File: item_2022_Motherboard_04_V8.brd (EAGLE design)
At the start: 160 x 100 mm, 50 parts, among them IC1 MCP602SN, IC2 LD117AS33TR, IC4 MCP6S26, U1 ESP32-DEVKITC-32D, U2 ADS1256_BOARD, U3 SSD1306_128X64, X1 MSTBA4, X2 MSTBA4

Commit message: aggiunta su sch condizionamento coppie
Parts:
- removed JP1: (no value), pinhead:1X08
- removed JP2: (no value), pinhead:2X04
- added C12, C13, C15, C20, C29: 100nF, rcl_LargePads:C0805
- added C14: 10uF / 16V, rcl_LargePads:PANASONIC_C
- added C16, C17, C18, C19: 3.3uF/50V, rcl_LargePads:C0805
- added C21, C23, C25, C27: 2.2uF, rcl_LargePads:C0805
- added C22, C24, C26, C28: 1uF, rcl_LargePads:C0805
- added C30: 100nF, rcl:C0805
- added D2, D3, D4, D5: BZW06-10B, diode_LargePads:F126Z12
- added GND, GND36: TPTP18SQ, testpad:TP18SQ
- added IC3: MCP1525TO, MCP1525_MCP1541:TO92
- added IC5, IC6, IC9: MCP6004SO, MCP6002_MCP6004:SO14
- added IC7: MCP3204SL, MCP3204_MCP3208:SO14
- added IC8: LM336LP, linear:TO92
- added R10, R11: 6.8k, rcl_LargePads:R0805
- added R12, R14, R22, R37, R39, R41, R43: 3.3k, rcl_LargePads:R0805
- added R13, R19, R21, R23: 5.6k, rcl_LargePads:R0805
- added R20: 3.3k, rcl_LargePads:M0805
- added R24, R26, R28, R30: 2.7k, rcl_LargePads:R0805
- added R25, R27, R29, R31: 82, rcl_LargePads:R0805
- added R32, R33, R34, R35: 1.8k, rcl_LargePads:R0805
- added R36, R38, R40, R42: 1.5k, rcl_LargePads:R0805
- added R44: 2.7k, rcl:R0805
- added R45, R46, R47, R48: 47, rcl:R0805
- added R49: 10k, rcl:R0805
- added TP13, TP7, TP8: TPTP16R, testpad:TP16R
- added TP14, TP15, TP16, TP17, TP18, TP19, TP20, TP21: TPTP14R, testpad:TP14R
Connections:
- removed net 3V3: U1.1
- removed net ADC_HALF_VREF: IC4.8, JP1.1, R16.1, R18.1, R2.1, R4.1, TP9.TP
- new net +2.5V: IC9.13, IC9.14, R32.1
- new net +3.3V_B: R49.2, U1.1
- new net ADC_HALF_VREF_A: IC4.8, IC9.8, IC9.9, R2.1, R4.1, TP13.TP, TP9.TP
- new net ADC_HALF_VREF_B: IC9.1, IC9.2, R16.1, R18.1
- new net ADC_VREF: IC7.13, IC9.6, IC9.7
- new net A_SPEED1: C25.2, IC6.8, IC6.9, IC7.3, TP20.TP
- new net A_SPEED2: C27.2, IC6.13, IC6.14, IC7.4, TP21.TP
- new net A_TORQUE1: C21.2, IC6.1, IC6.2, IC7.1, TP18.TP
- new net A_TORQUE2: C23.2, IC6.6, IC6.7, IC7.2, TP19.TP
- new net EN/!RESET!: C30.2, R49.1, U1.2
- new net N$1: C15.1, IC9.10, IC9.3, R10.1, R11.2
- new net N$15: R12.1, R13.2
- new net N$16: R14.1, R19.2
- new net N$17: R20.1, R21.2
- new net N$18: R22.1, R23.2
- new net N$19: R24.2, R25.1
- new net N$20: C16.1, IC5.3, R13.1, R24.1, R32.2, TP14.TP
- new net N$22: R26.2, R27.1
- new net N$23: R28.2, R29.1
- new net N$24: R30.2, R31.1
- new net N$25: C17.1, IC5.5, R19.1, R26.1, R33.2, TP15.TP
- new net N$26: C18.1, IC5.10, R21.1, R28.1, R34.2, TP16.TP
- new net N$27: C19.1, IC5.12, R23.1, R30.1, R35.2, TP17.TP
- new net N$28: IC5.1, IC5.2, R36.1
- new net N$29: IC5.6, IC5.7, R38.1
- new net N$30: IC5.8, IC5.9, R40.1
- new net N$31: IC5.13, IC5.14, R42.1
- new net N$32: C21.1, R36.2, R37.1
- new net N$33: C22.1, IC6.3, R37.2
- new net N$34: C23.1, R38.2, R39.1
- new net N$35: C24.1, IC6.5, R39.2
- new net N$36: C25.1, R40.2, R41.1
- new net N$37: C26.1, IC6.10, R41.2
- new net N$38: C27.1, R42.2, R43.1
- new net N$39: C28.1, IC6.12, R43.2
- new net N$40: R48.1, U1.27
- new net N$41: IC7.11, R45.1
- new net N$42: IC7.9, R46.1
- new net N$43: IC7.8, R47.1
- new net VREF: C14.+, IC3.2, IC8.2, IC9.12, IC9.5, R10.2, R44.1, TP8.TP
- net !CS_MCP3204!: now also R47.2; no longer JP1.5
- net +3V3: now also C29.1, IC7.14; no longer JP1.2
- net +5V: now also C12.1, C13.1, C20.1, IC3.3, IC5.4, IC6.4, IC9.4, R44.2, TP7.TP; no longer JP1.3
- net GND: now also C12.2, C13.2, C14.-, C15.2, C16.2, C17.2, C18.2, C19.2, C20.2, C22.2, C24.2, C26.2, C28.2, C29.2, D2.C, D3.C, D4.C, D5.C, GND.TP, GND36.TP, IC3.1, IC5.11, IC6.11, IC7.12, IC7.7, IC8.3, IC9.11, R11.1, R25.2, R27.2, R29.2, R31.2; no longer JP1.4
- net SPEED1+: now also D3.A, R20.2; no longer JP2.6
- net SPEED1-: no longer JP2.5
- net SPEED2+: now also D4.A, R22.2; no longer JP2.8
- net SPEED2-: no longer JP2.7
- net TORQUE1+: now also D5.A, R12.2; no longer JP2.2
- net TORQUE1-: no longer JP2.1
- net TORQUE2+: now also D2.A, R14.2; no longer JP2.4
- net TORQUE2-: no longer JP2.3
- net VSPI_MISO: now also IC7.10, R48.2; no longer JP1.7, U1.27
- net VSPI_MOSI: now also R46.2; no longer JP1.8
- net VSPI_SCK: now also R45.2; no longer JP1.6
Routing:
- net ADC_HALF_VREF: track 144.2 -> 0.00 mm, vias 5 -> 0
- net ADC_HALF_VREF_A: track 0.00 -> 144.2 mm, vias 0 -> 5

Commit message: aggiunta su brd cond coppie da sbrogliare
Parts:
- moved R47 266.2 mm to (157.6, 75.8), turned to 90 degrees
- moved R46 259.5 mm to (153.7, 75.8), turned to 90 degrees
- moved R45 252.7 mm to (149.8, 75.8), turned to 90 degrees
- moved TP7 237.9 mm to (121.9, 86.9)
- moved C30 235.8 mm to (21.3, 85.6), turned to 90 degrees
- moved R49 234.5 mm to (21.5, 89.7), turned to 90 degrees
- moved R42 227.9 mm to (151.1, 50.8), turned to 90 degrees
- moved R43 227.3 mm to (151.1, 55.2), turned to 90 degrees
- moved C29 225.9 mm to (142.3, 68.8), turned to 90 degrees
- moved TP13 223.0 mm to (124.4, 62.8)
- moved R48 221.3 mm to (46.5, 77.4), turned to 90 degrees
- moved GND 217.1 mm to (154.7, 84.4)
- moved C14 215.8 mm to (123.2, 82.5), turned to 180 degrees
- moved R44 213.1 mm to (118.7, 67.3), turned to 90 degrees
- moved TP8 210.5 mm to (119.1, 59.6)
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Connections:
- removed net SPEED1-: PL1.11
- removed net SPEED2-: PL1.13
- removed net TORQUE1-: PL1.7
- removed net TORQUE2-: PL1.9
- net +2.5V: now also R33.1, R34.1, R35.1
- net GND: now also C30.1, PL1.11, PL1.13, PL1.7, PL1.9
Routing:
- net SPEED2-: track 142.9 -> 0.00 mm, vias 1 -> 0
- net TORQUE1-: track 128.9 -> 0.00 mm, vias 2 -> 0
- net SPEED1-: track 122.9 -> 0.00 mm
- net TORQUE2-: track 118.3 -> 0.00 mm, vias 3 -> 0
- net SPEED2+: track 115.6 -> 0.00 mm, vias 2 -> 0
- net SPEED1+: track 109.6 -> 0.00 mm, vias 1 -> 0
- net TORQUE2+: track 107.0 -> 0.00 mm, vias 1 -> 0
- net TORQUE1+: track 96.3 -> 0.00 mm, vias 2 -> 0
- net VSPI_MISO: track 203.6 -> 124.8 mm
- net GND: track 792.1 -> 716.3 mm
- net VSPI_MOSI: track 241.5 -> 188.5 mm
- net ADC_HALF_VREF_A: track 144.2 -> 104.9 mm
- net +5V: track 195.0 -> 179.3 mm
- net +3V3: track 249.1 -> 241.9 mm
- removed copper zone on layer 1, net GND
- removed copper zone on layer 16, net GND
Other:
- board text removed: "CONDIZIONAMENTO COPPIE - VELOCITA'"

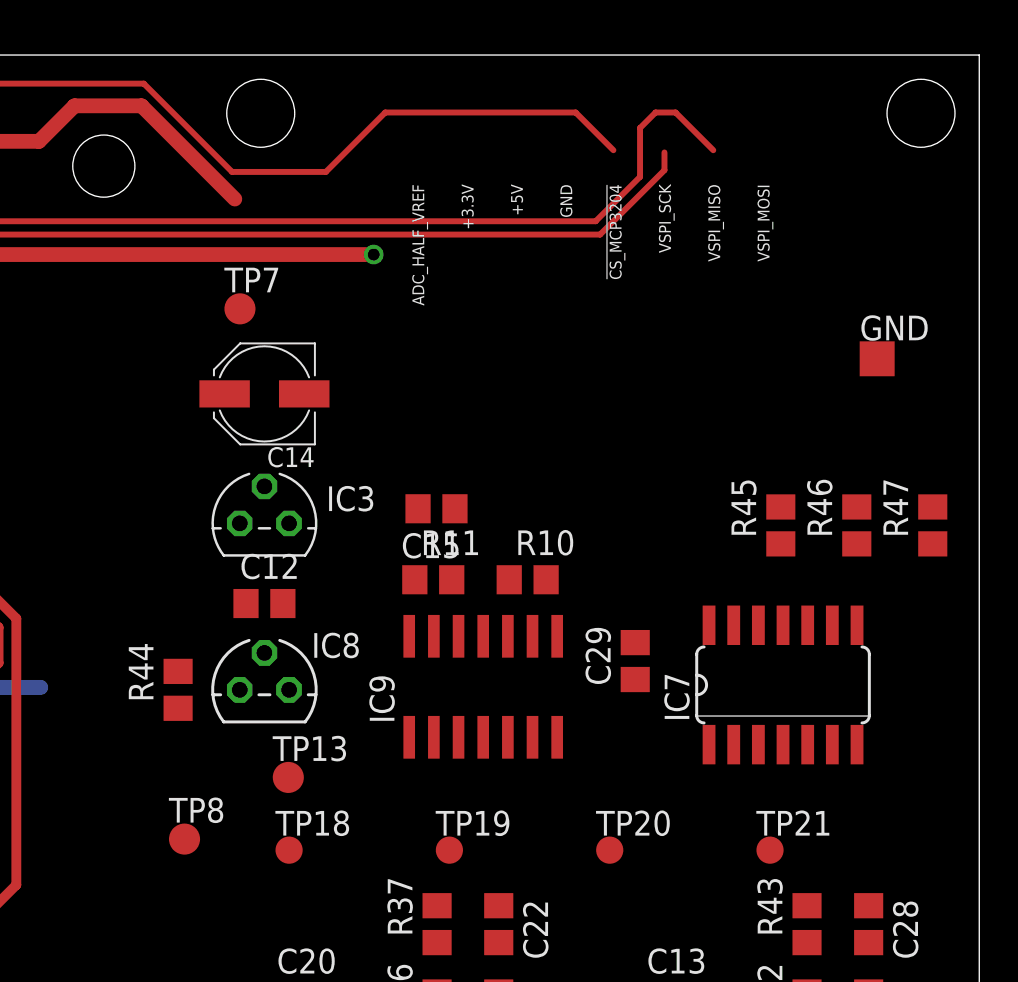
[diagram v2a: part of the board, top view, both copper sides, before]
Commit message: place pcb components on grid
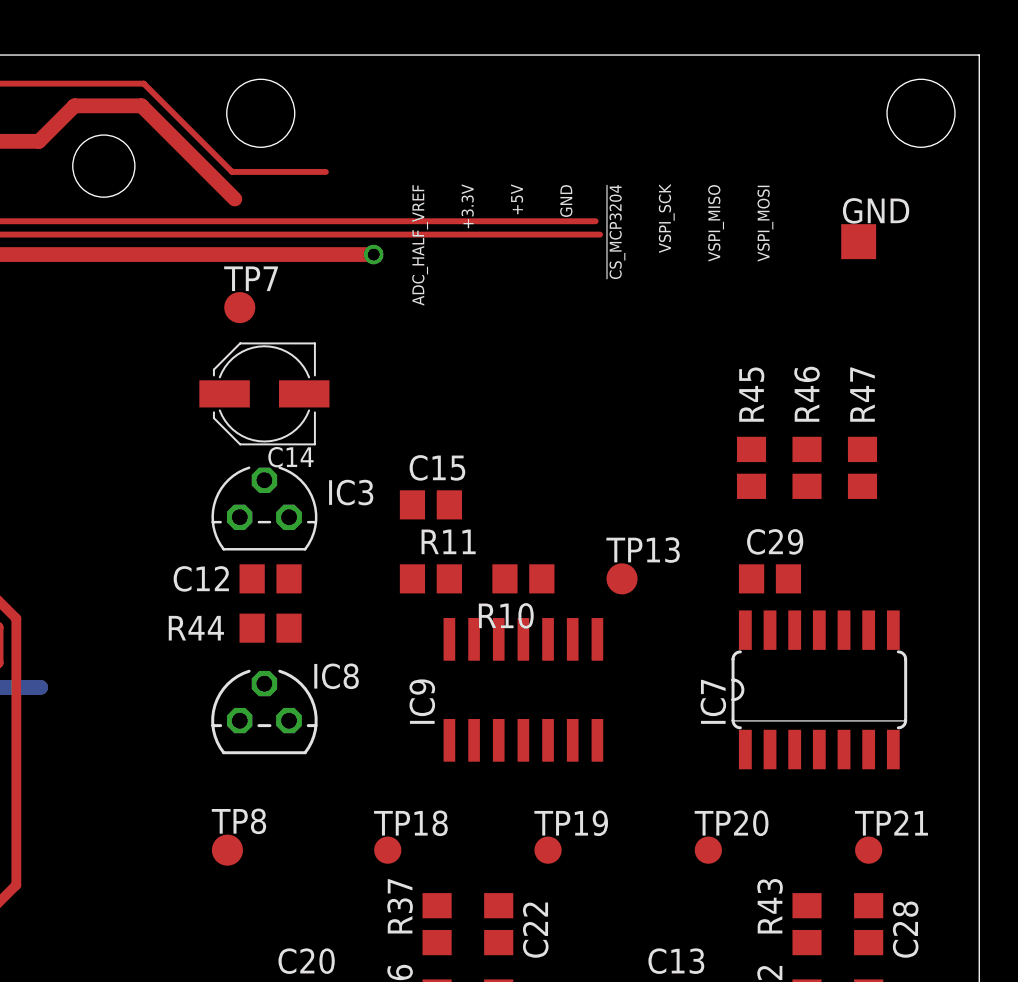
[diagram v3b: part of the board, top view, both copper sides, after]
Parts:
- moved TP13 20.0 mm to (141.6, 73.0)
- moved C29 8.13 mm to (149.2, 73.0), turned to 0 degrees
- moved GND 6.11 mm to (153.8, 90.4)
- moved R44 5.72 mm to (123.5, 70.5), turned to 180 degrees
- moved TP20 5.08 mm to (146.1, 59.1)
- moved TP21 5.08 mm to (154.3, 59.1)
- moved TP18 5.08 mm to (129.5, 59.1)
- moved TP19 5.08 mm to (137.8, 59.1)
- moved R47 4.68 mm to (154.0, 78.7)
- moved R46 3.92 mm to (151.1, 78.7)
- moved R45 3.32 mm to (148.3, 78.7)
- moved TP8 2.28 mm to (121.3, 59.1)
- moved IC9 2.08 mm to (136.5, 67.3)
- moved IC7 1.89 mm to (151.8, 67.3)
- moved IC8 1.59 mm to (123.2, 65.7)
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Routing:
- net !CS_MCP3204!: track 167.4 -> 150.5 mm
- net VSPI_MISO: track 124.8 -> 114.2 mm
- net VSPI_SCK: track 223.6 -> 218.0 mm

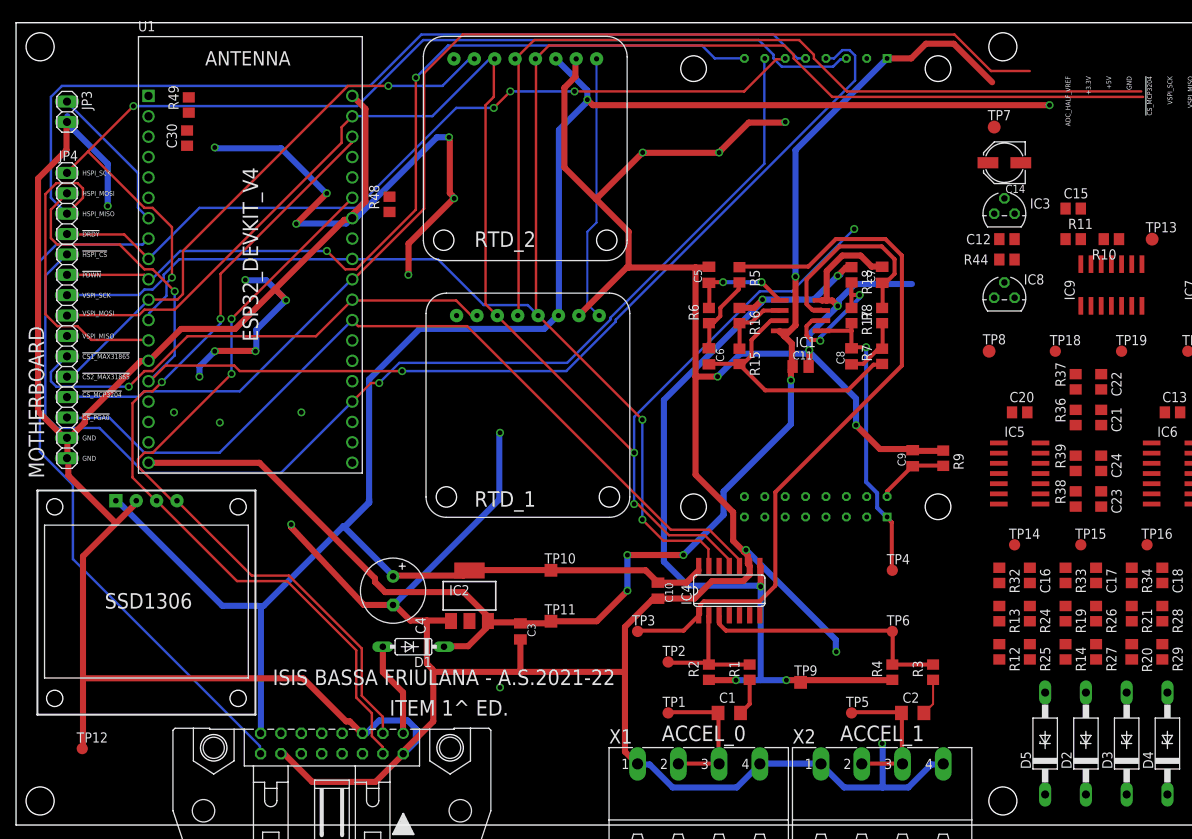
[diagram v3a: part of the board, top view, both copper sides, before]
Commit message: changed PGA inputs
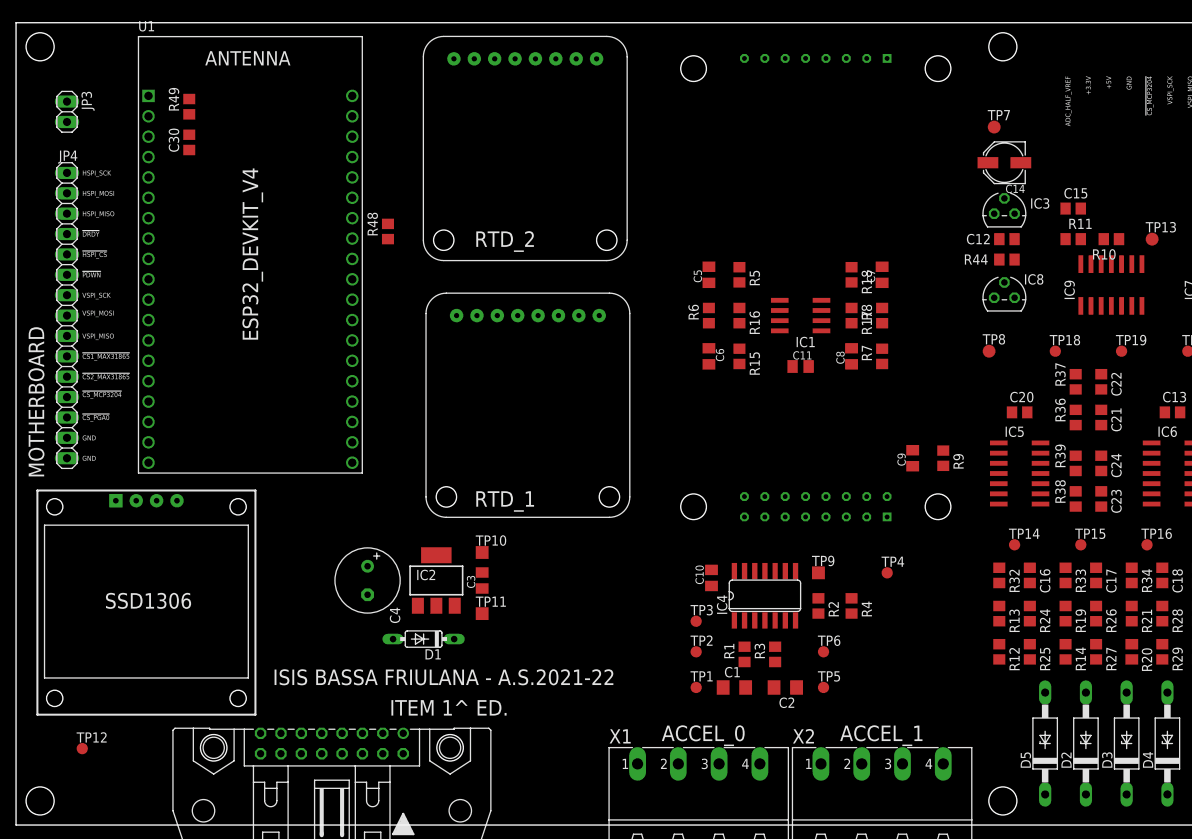
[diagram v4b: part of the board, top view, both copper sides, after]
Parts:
- moved R3 19.8 mm to (94.6, 21.3)
- moved C2 16.2 mm to (95.9, 17.1), turned to 180 degrees
- moved R2 16.0 mm to (100.0, 27.3), turned to 270 degrees
- moved TP9 13.8 mm to (100.0, 31.4)
- moved R4 9.69 mm to (104.1, 27.3), turned to 270 degrees
- moved TP6 8.94 mm to (100.6, 21.6)
- moved TP10 8.86 mm to (58.1, 34.0)
- moved TP11 8.63 mm to (58.1, 26.4)
- moved C3 7.94 mm to (58.1, 30.5), turned to 90 degrees
- moved TP3 7.41 mm to (84.8, 25.4)
- moved C10 6.85 mm to (86.7, 30.8)
- moved TP5 4.72 mm to (100.6, 17.1)
- moved TP1 4.72 mm to (84.8, 17.1)
- moved IC2 4.55 mm to (52.4, 30.5)
- moved IC4 4.49 mm to (93.3, 28.6)
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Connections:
- net GND: now also IC4.2, IC4.4, IC4.6, IC4.7
- net N$14: now also IC4.5; no longer IC4.3
- net N$4: now also IC4.3; no longer IC4.2
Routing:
- net GND: track 716.3 -> 0.00 mm, vias 28 -> 0
- net +3V3: track 241.9 -> 0.00 mm, vias 2 -> 0
- net VSPI_SCK: track 218.0 -> 0.00 mm, vias 2 -> 0
- net VSPI_MOSI: track 188.5 -> 0.00 mm, vias 3 -> 0
- net +5V: track 179.3 -> 0.00 mm, vias 5 -> 0
- net HSPI_MISO: track 152.6 -> 0.00 mm
- net !CS_MCP3204!: track 150.5 -> 0.00 mm
- net HSPI_MOSI: track 149.0 -> 0.00 mm, vias 2 -> 0
- net !HSPI_CS!: track 143.1 -> 0.00 mm, vias 1 -> 0
- net HSPI_SCK: track 133.3 -> 0.00 mm, vias 2 -> 0
- net VSPI_MISO: track 114.2 -> 0.00 mm
- net !PDWN!: track 109.0 -> 0.00 mm, vias 2 -> 0
- net !CS_PGA0!: track 105.7 -> 0.00 mm
- net I2C_SCL: track 105.5 -> 0.00 mm, vias 2 -> 0
- net ADC_HALF_VREF_A: track 104.9 -> 0.00 mm, vias 5 -> 0
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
